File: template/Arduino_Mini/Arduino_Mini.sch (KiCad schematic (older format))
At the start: 6 parts, among them P1 ADC, P2 Digital, P3 ADC, P4 COM, P5 Analog, P6 PWR

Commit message: rebuilt shematic and fix librairie
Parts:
- removed P1, P3: ADC, Socket_Arduino_Mini:Socket_Strip_Arduino_1x02, symbol CONN_2
- removed P2: Digital, Socket_Arduino_Mini:Socket_Strip_Arduino_1x12, symbol CONN_12
- removed P4: COM, Socket_Arduino_Mini:Socket_Strip_Arduino_1x05, symbol CONN_5
- removed P5: Analog, Socket_Arduino_Mini:Socket_Strip_Arduino_1x12, symbol CONN_12
- removed P6: PWR, Socket_Arduino_Mini:Socket_Strip_Arduino_1x02, symbol CONN_2
- added P1, P3: ADC, Socket_Arduino_Mini:Socket_Strip_Arduino_1x02, symbol CONN_01X02
- added P2: Digital, Socket_Arduino_Mini:Socket_Strip_Arduino_1x12, symbol CONN_01X12
- added P4: COM, Socket_Arduino_Mini:Socket_Strip_Arduino_1x05, symbol CONN_01X05
- added P5: Analog, Socket_Arduino_Mini:Socket_Strip_Arduino_1x12, symbol CONN_01X12
- added P6: PWR, Socket_Arduino_Mini:Socket_Strip_Arduino_1x02, symbol CONN_01X02
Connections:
- wire segments 41 -> 31
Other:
- note added: "1"

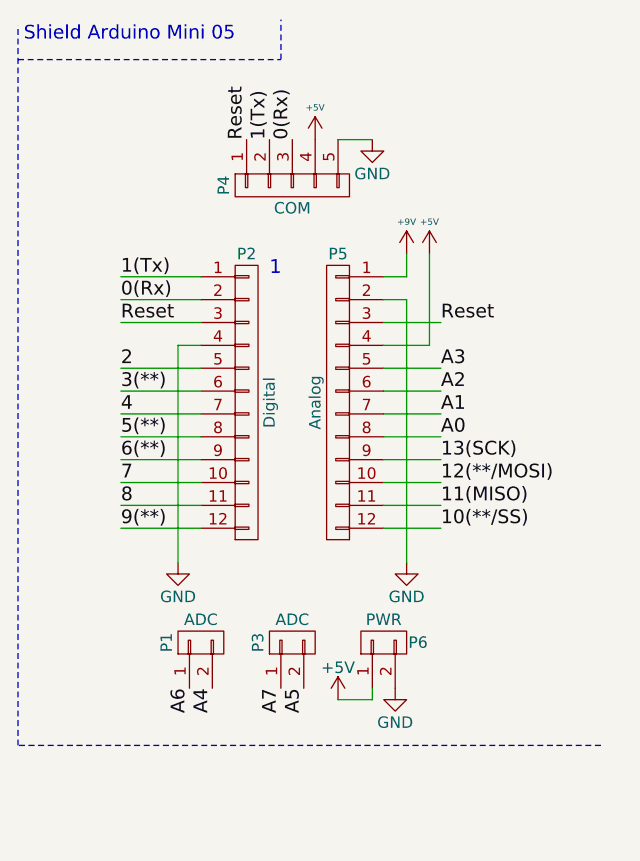
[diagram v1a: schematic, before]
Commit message: Fix pin order SS, MOSI, MISO, SCK
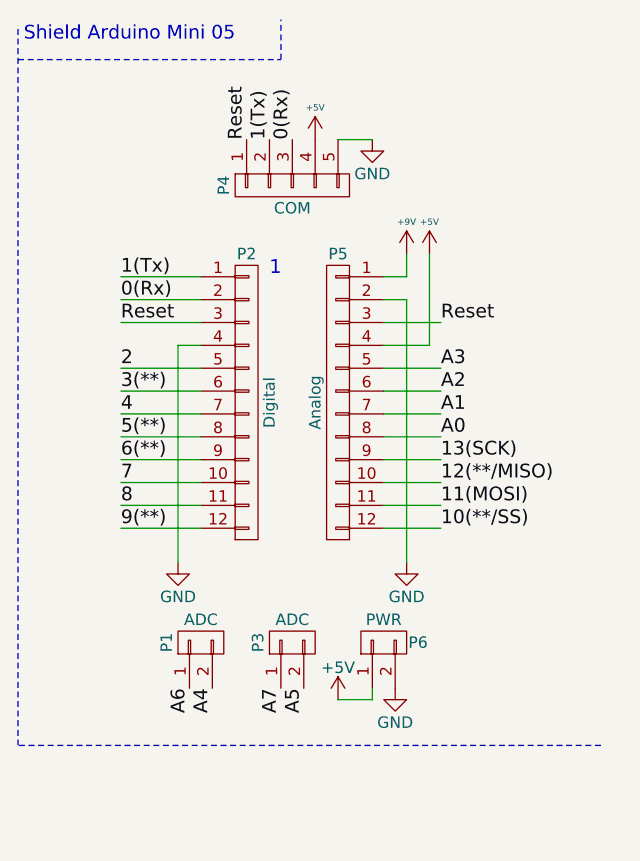
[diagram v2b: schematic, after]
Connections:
- net 11(MISO) renamed 11(MOSI)
- net 12(**/MOSI) renamed 12(**/MISO)
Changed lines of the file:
@@
 10(**/SS)
 Text Label 10500 2600 0    60   ~ 0
-11(MISO)
+11(MOSI)
 Text Label 10500 2500 0    60   ~ 0
-12(**/MOSI)
+12(**/MISO)
 Text Label 10500 2400 0    60   ~ 0
 13(SCK)

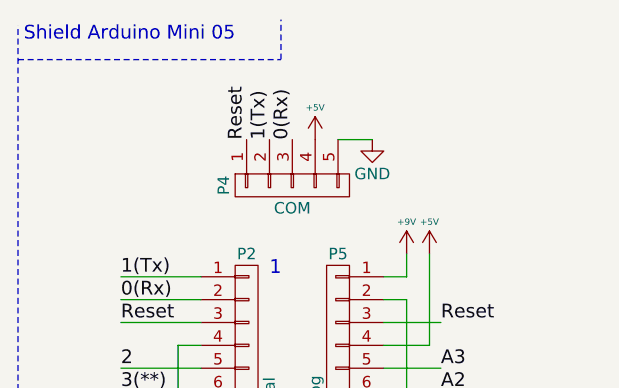
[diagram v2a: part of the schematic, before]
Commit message: On Template Arduino_Mini change connector P4 pin 1 : rst to 7
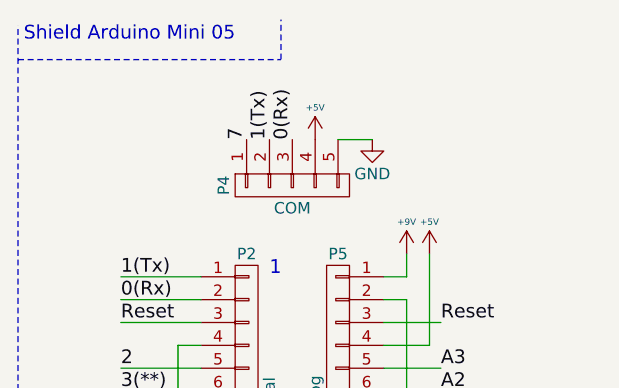
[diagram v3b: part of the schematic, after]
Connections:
- net 7: now also P4.1 (P1)
- net Reset: no longer P4.1 (P1)
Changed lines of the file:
@@
 0(Rx)
 Text Label 9650 1000 1    60   ~ 0
-Reset
+7
 Text Label 9400 3400 3    60   ~ 0
 A6
